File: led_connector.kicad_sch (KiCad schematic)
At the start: 7 parts, among them U3 SM02B-SRSS-TB-LF-SN, U4 SM02B-SRSS-TB-LF-SN

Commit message: Update naming convention
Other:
- title: (none) -> LZ1 OSRAM LuxiGen LED Driver
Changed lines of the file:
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@@
 (kicad_sch (version 20211123) (generator eeschema)
   (paper "A4")
+  (title_block
+    (title "LZ1 OSRAM LuxiGen LED Driver")
+    (date "2023-05-04")
+    (rev "1.0.0")
+    (comment 1 "www.antmicro.com")
+  )
   (junction (at 60.325 114.935) (diameter 0) (color 0 0 0 0)
   )
@@
   (symbol (lib_id "power:GND") (at 60.325 116.205 0) (unit 1)
     (in_bom yes) (on_board yes) (fields_autoplaced)
-    (property "Reference" "#PWR0103" (id 0) (at 60.325 122.555 0)
+    (property "Reference" "#PWR?" (id 0) (at 60.325 122.555 0)
       (effects (font (size 1.27 1.27)) hide)
     )
@@
   (symbol (lib_id "power:GND") (at 219.71 114.935 0) (unit 1)
     (in_bom yes) (on_board yes) (fields_autoplaced)
-    (property "Reference" "#PWR0102" (id 0) (at 219.71 121.285 0)
-      (effects (font (size 1.27 1.27)) hide)
-    )
+    (property "Reference" "#PWR?" (id 0) (at 219.71 121.285 0)
+      (effects (font (size 1.27 1.27)) hide)
+    )

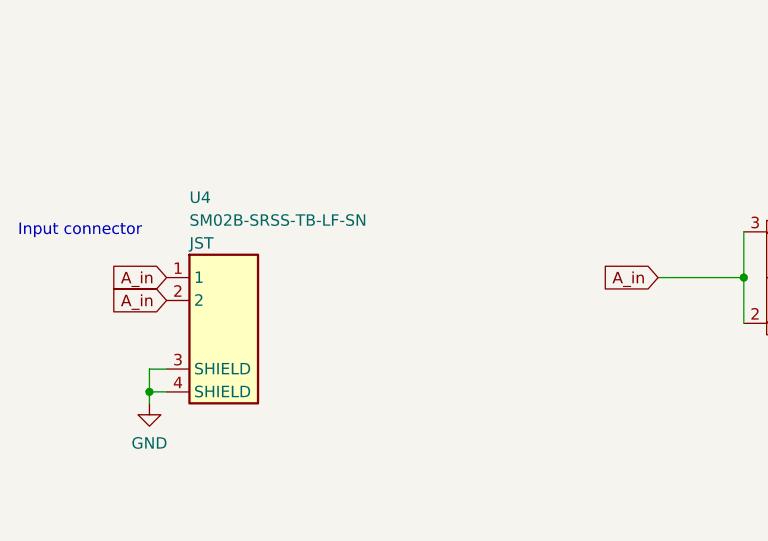
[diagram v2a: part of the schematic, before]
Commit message: Correct sch logos. Update PCB from schematic
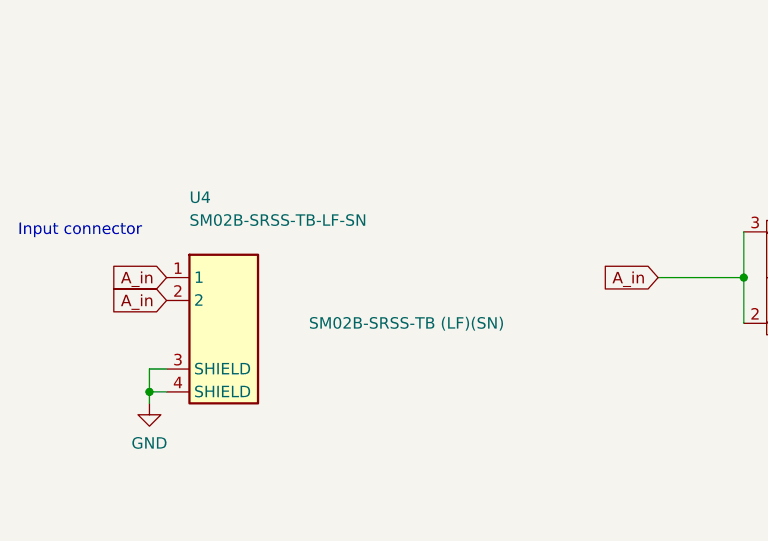
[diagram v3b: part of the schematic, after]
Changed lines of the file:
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@@
   (symbol (lib_id "power:GND") (at 60.325 116.205 0) (unit 1)
     (in_bom yes) (on_board yes) (fields_autoplaced)
-    (property "Reference" "#PWR?" (id 0) (at 60.325 122.555 0)
+    (property "Reference" "#PWR0102" (id 0) (at 60.325 122.555 0)
       (effects (font (size 1.27 1.27)) hide)
     )
@@
   (symbol (lib_id "power:GND") (at 219.71 114.935 0) (unit 1)
     (in_bom yes) (on_board yes) (fields_autoplaced)
-    (property "Reference" "#PWR?" (id 0) (at 219.71 121.285 0)
+    (property "Reference" "#PWR0103" (id 0) (at 219.71 121.285 0)
       (effects (font (size 1.27 1.27)) hide)
     )
@@
       (effects (font (size 1.27 1.27)) hide)
     )
-    (property "MPN" "SM02B-SRSS-TB (LF)(SN)" (id 4) (at 88.9 107.315 0)
-      (effects (font (size 1.27 1.27)) hide)
-    )
+    (property "MPN" "SM02B-SRSS-TB (LF)(SN)" (id 4) (at 88.9 107.315 0))
     (property "Manufacturer" "JST" (id 5) (at 64.77 98.4249 0)
-      (effects (font (size 1.27 1.27)) (justify left))
+      (effects (font (size 1.27 1.27)) (justify left) hide)
     )
     (property "Copyright" "Copyright (c) 2023 Antmicro" (id 6) (at 90.17 109.855 0)

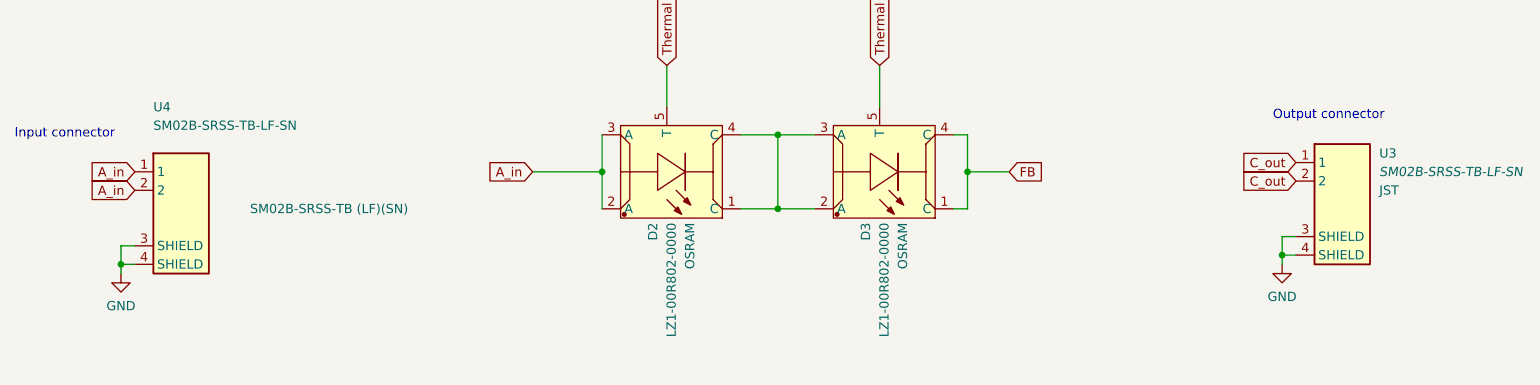
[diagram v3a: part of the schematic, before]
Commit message: Correct symbols and footprints with missing 3D models
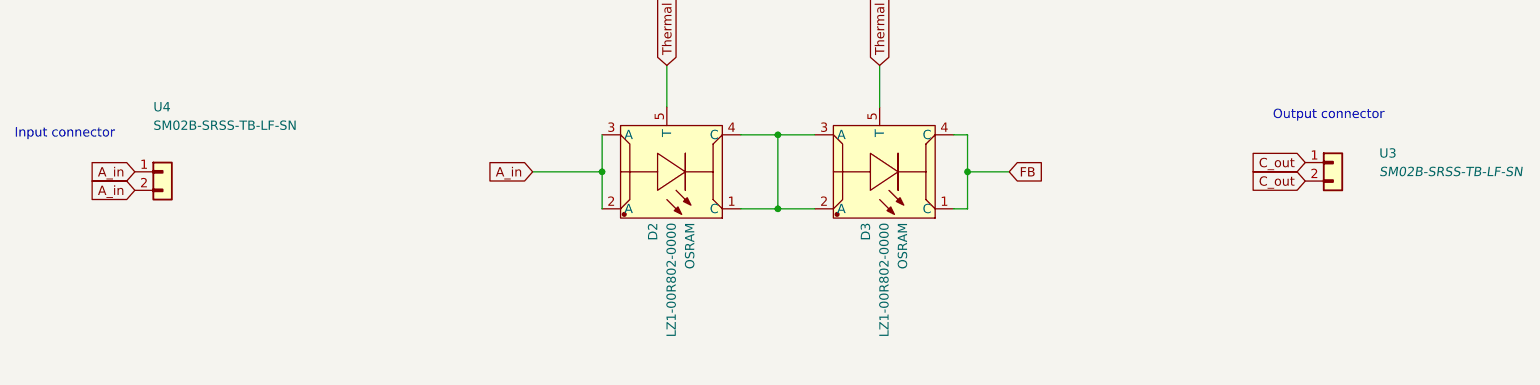
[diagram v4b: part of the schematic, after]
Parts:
- U3, U4: footprint antmicro-footprints:JST_SM02B-SRSS-TB(LF)(SN) -> antmicro-footprints:JST_SM02B-SRSS-TB-LF-SN; Author (none) -> Antmicro; Copyright Copyright (c) 2023 Antmicro -> (none); License Apache-2.0 License -> Apache-2.0; MPN SM02B-SRSS-TB (LF)(SN) -> SM02B-SRSS-TB(LF)(SN)
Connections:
- removed net GND: U3.3 (SHIELD), U3.4 (SHIELD), U4.3 (SHIELD), U4.4 (SHIELD)
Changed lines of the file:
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@@
     (comment 1 "www.antmicro.com")
   )
-  (junction (at 60.325 114.935) (diameter 0) (color 0 0 0 0)
-  )
   (junction (at 144.145 39.37) (diameter 0) (color 0 0 0 0)
   )
   (junction (at 156.21 52.705) (diameter 0) (color 0 0 0 0)
   )
-  (junction (at 219.71 113.665) (diameter 0) (color 0 0 0 0)
-  )
   (junction (at 176.53 102.235) (diameter 0) (color 0 0 0 0)
   )
@@
     (stroke (width 0) (type default) (color 0 0 0 0))
   )
-  (wire (pts (xy 219.71 113.665) (xy 221.615 113.665))
-    (stroke (width 0) (type default) (color 0 0 0 0))
-  )
   (wire (pts (xy 145.415 97.155) (xy 150.495 97.155))
     (stroke (width 0) (type default) (color 0 0 0 0))
@@
     (stroke (width 0) (type default) (color 0 0 0 0))
   )
-  (wire (pts (xy 219.71 113.665) (xy 219.71 114.935))
-    (stroke (width 0) (type default) (color 0 0 0 0))
-  )
   (polyline (pts (xy 163.195 17.78) (xy 163.195 31.115))
     (stroke (width 0) (type default) (color 0 0 0 0))
@@
     (stroke (width 0) (type default) (color 0 0 0 0))
   )
-  (wire (pts (xy 219.71 111.125) (xy 219.71 113.665))
-    (stroke (width 0) (type default) (color 0 0 0 0))
-  )
   (wire (pts (xy 150.495 97.155) (xy 150.495 107.315))
     (stroke (width 0) (type default) (color 0 0 0 0))
@@
     (stroke (width 0) (type default) (color 0 0 0 0))
   )
-  (wire (pts (xy 60.325 114.935) (xy 62.23 114.935))
-    (stroke (width 0) (type default) (color 0 0 0 0))
-  )
   (wire (pts (xy 176.53 107.315) (xy 176.53 102.235))
     (stroke (width 0) (type default) (color 0 0 0 0))
@@
     (stroke (width 0) (type default) (color 0 0 0 0))
   )
-  (wire (pts (xy 60.325 112.395) (xy 60.325 114.935))
-    (stroke (width 0) (type default) (color 0 0 0 0))
-  )
   (wire (pts (xy 144.145 39.37) (xy 144.145 45.085))
     (stroke (width 0) (type default) (color 0 0 0 0))
@@
     (stroke (width 0) (type default) (color 0 0 0 0))
   )
-  (wire (pts (xy 62.23 112.395) (xy 60.325 112.395))
-    (stroke (width 0) (type default) (color 0 0 0 0))
-  )
   (polyline (pts (xy 154.305 17.78) (xy 154.305 31.115))
     (stroke (width 0) (type default) (color 0 0 0 0))
@@
     (stroke (width 0) (type default) (color 0 0 0 0))
   )
-  (wire (pts (xy 221.615 111.125) (xy 219.71 111.125))
-    (stroke (width 0) (type default) (color 0 0 0 0))
-  )
   (wire (pts (xy 156.21 45.085) (xy 156.21 52.705))
     (stroke (width 0) (type default) (color 0 0 0 0))
@@
   )
   (wire (pts (xy 126.365 107.315) (xy 126.365 102.235))
-    (stroke (width 0) (type default) (color 0 0 0 0))
-  )
-  (wire (pts (xy 60.325 114.935) (xy 60.325 116.205))
     (stroke (width 0) (type default) (color 0 0 0 0))
   )
@@
     )
   )
-  (global_label "C_out" (shape input) (at 221.615 100.965 180) (fields_autoplaced)
-    (effects (font (size 1.27 1.27)) (justify right))
-    (property "Intersheet References" "${INTERSHEET_REFS}" (id 0) (at 213.9405 100.8856 0)
+  (global_label "C_out" (shape input) (at 222.885 100.965 180) (fields_autoplaced)
+    (effects (font (size 1.27 1.27)) (justify right))
+    (property "Intersheet References" "${INTERSHEET_REFS}" (id 0) (at 215.2105 100.8856 0)
       (effects (font (size 1.27 1.27)) (justify right) hide)
     )
@@
     )
   )
-  (global_label "C_out" (shape input) (at 221.615 103.505 180) (fields_autoplaced)
-    (effects (font (size 1.27 1.27)) (justify right))
-    (property "Intersheet References" "${INTERSHEET_REFS}" (id 0) (at 213.9405 103.4256 0)
+  (global_label "C_out" (shape input) (at 222.885 103.505 180) (fields_autoplaced)
+    (effects (font (size 1.27 1.27)) (justify right))
+    (property "Intersheet References" "${INTERSHEET_REFS}" (id 0) (at 215.2105 103.4256 0)
       (effects (font (size 1.27 1.27)) (justify right) hide)
     )
@@
     (pin "5")
   )
-  (symbol (lib_id "power:GND") (at 60.325 116.205 0) (unit 1)
-    (in_bom yes) (on_board yes) (fields_autoplaced)
-    (property "Reference" "#PWR0102" (id 0) (at 60.325 122.555 0)
-      (effects (font (size 1.27 1.27)) hide)
-    )
-    (property "Value" "GND" (id 1) (at 60.325 120.65 0))
-    (property "Footprint" "" (id 2) (at 60.325 116.205 0)
-      (effects (font (size 1.27 1.27)) hide)
-    )
-    (property "Datasheet" "" (id 3) (at 60.325 116.205 0)
-      (effects (font (size 1.27 1.27)) hide)
-    )
-    (pin "1")
-  )
   (symbol (lib_id "antmicroRectangularConnectorsHeadersMalePins:SM02B-SRSS-TB-LF-SN") (at 222.885 100.965 0) (unit 1)
     (in_bom yes) (on_board yes) (fields_autoplaced)
@@
       (effects (font (size 1.27 1.27) italic) (justify left))
     )
-    (property "Footprint" "antmicro-footprints:JST_SM02B-SRSS-TB(LF)(SN)" (id 2) (at 260.985 111.125 0)
-      (effects (font (size 1.27 1.27)) hide)
-    )
-    (property "Datasheet" "https://www.farnell.com/datasheets/2082363.pdf" (id 3) (at 260.985 103.505 0)
-      (effects (font (size 1.27 1.27)) hide)
-    )
-    (property "MPN" "SM02B-SRSS-TB (LF)(SN)" (id 4) (at 249.555 106.045 0)
-      (effects (font (size 1.27 1.27)) hide)
-    )
-    (property "Manufacturer" "JST" (id 5) (at 233.045 104.7749 0)
-      (effects (font (size 1.27 1.27)) (justify left))
-    )
-    (property "Copyright" "Copyright (c) 2023 Antmicro" (id 6) (at 250.825 108.585 0)
-      (effects (font (size 1.27 1.27)) hide)
-    )
-    (property "License" "Apache-2.0 License" (id 7) (at 247.015 100.965 0)
-      (effects (font (size 1.27 1.27)) hide)
-    )
-    (pin "1")
-    (pin "2")
-    (pin "3")
-    (pin "4")
-  )
-  (symbol (lib_id "power:GND") (at 219.71 114.935 0) (unit 1)
-    (in_bom yes) (on_board yes) (fields_autoplaced)
-    (property "Reference" "#PWR0103" (id 0) (at 219.71 121.285 0)
-      (effects (font (size 1.27 1.27)) hide)
-    )
-    (property "Value" "GND" (id 1) (at 219.71 119.38 0))
-    (property "Footprint" "" (id 2) (at 219.71 114.935 0)
-      (effects (font (size 1.27 1.27)) hide)
-    )
-    (property "Datasheet" "" (id 3) (at 219.71 114.935 0)
-      (effects (font (size 1.27 1.27)) hide)
-    )
-    (pin "1")
+    (property "Footprint" "antmicro-footprints:JST_SM02B-SRSS-TB-LF-SN" (id 2) (at 249.555 109.855 0)
+      (effects (font (size 1.27 1.27) (thickness 0.15)) (justify left bottom) hide)
+    )
+    (property "Datasheet" "https://www.jst-mfg.com/product/pdf/eng/eSH.pdf" (id 3) (at 249.555 112.395 0)
+      (effects (font (size 1.27 1.27) (thickness 0.15)) (justify left bottom) hide)
+    )
+    (property "MPN" "SM02B-SRSS-TB(LF)(SN)" (id 4) (at 249.555 114.935 0)
+      (effects (font (size 1.27 1.27) (thickness 0.15)) (justify left bottom) hide)
+    )
+    (property "Manufacturer" "JST" (id 5) (at 249.555 117.475 0)
+      (effects (font (size 1.27 1.27) (thickness 0.15)) (justify left bottom) hide)
+    )
+    (property "License" "Apache-2.0" (id 7) (at 249.555 122.555 0)
+      (effects (font (size 1.27 1.27) (thickness 0.15)) (justify left bottom) hide)
+    )
+    (property "Author" "Antmicro" (id 7) (at 249.555 120.015 0)
+      (effects (font (size 1.27 1.27) (thickness 0.15)) (justify left bottom) hide)
+    )
+    (pin "1")
+    (pin "2")
   )
   (symbol (lib_id "antmicroLEDIndicationDiscrete:LZ1-00R802-0000") (at 145.415 107.315 180) (unit 1)
@@
       (effects (font (size 1.27 1.27)) (justify left))
     )
-    (property "Footprint" "antmicro-footprints:JST_SM02B-SRSS-TB(LF)(SN)" (id 2) (at 100.33 112.395 0)
-      (effects (font (size 1.27 1.27)) hide)
-    )
-    (property "Datasheet" "https://www.farnell.com/datasheets/2082363.pdf" (id 3) (at 100.33 104.775 0)
-      (effects (font (size 1.27 1.27)) hide)
-    )
-    (property "MPN" "SM02B-SRSS-TB (LF)(SN)" (id 4) (at 88.9 107.315 0))
-    (property "Manufacturer" "JST" (id 5) (at 64.77 98.4249 0)
-      (effects (font (size 1.27 1.27)) (justify left) hide)
-    )
-    (property "Copyright" "Copyright (c) 2023 Antmicro" (id 6) (at 90.17 109.855 0)
-      (effects (font (size 1.27 1.27)) hide)
-    )
-    (property "License" "Apache-2.0 License" (id 7) (at 86.36 102.235 0)
-      (effects (font (size 1.27 1.27)) hide)
-    )
-    (pin "1")
-    (pin "2")
-    (pin "3")
-    (pin "4")
+    (property "Footprint" "antmicro-footprints:JST_SM02B-SRSS-TB-LF-SN" (id 2) (at 88.9 111.125 0)
+      (effects (font (size 1.27 1.27) (thickness 0.15)) (justify left bottom) hide)
+    )
+    (property "Datasheet" "https://www.jst-mfg.com/product/pdf/eng/eSH.pdf" (id 3) (at 88.9 113.665 0)
+      (effects (font (size 1.27 1.27) (thickness 0.15)) (justify left bottom) hide)
+    )
+    (property "MPN" "SM02B-SRSS-TB(LF)(SN)" (id 4) (at 88.9 116.205 0)
+      (effects (font (size 1.27 1.27) (thickness 0.15)) (justify left bottom) hide)
+    )
+    (property "Manufacturer" "JST" (id 5) (at 88.9 118.745 0)
+      (effects (font (size 1.27 1.27) (thickness 0.15)) (justify left bottom) hide)
+    )
+    (property "License" "Apache-2.0" (id 7) (at 88.9 123.825 0)
+      (effects (font (size 1.27 1.27) (thickness 0.15)) (justify left bottom) hide)
+    )
+    (property "Author" "Antmicro" (id 7) (at 88.9 121.285 0)
+      (effects (font (size 1.27 1.27) (thickness 0.15)) (justify left bottom) hide)
+    )
+    (pin "1")
+    (pin "2")
   )
 )

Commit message: Refresh standardization on schematic and PCB
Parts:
- D2, D3: footprint antmicro-footprints:LZ1-00R802_4EP_4.4x4.4 -> antmicro-footprints:LED_IR_LZ1-00R802; symbol antmicroLEDIndicationDiscrete:LZ1-00R802-0000 -> antmicroLEDIndicationDiscrete:LED_IR_LZ1-00R802; Author (none) -> Antmicro; License Apache-2.0 License -> Apache-2.0; Manufacturer OSRAM -> Osram
- R10, R11, R7: Author (none) -> Antmicro; Copyright Copyright (c) 2023 Antmicro -> (none); License Apache-2.0 License -> Apache-2.0; Manufacturer Multicomp PRO -> Multicomp
- renumbered U3 to J3, U4 to J4

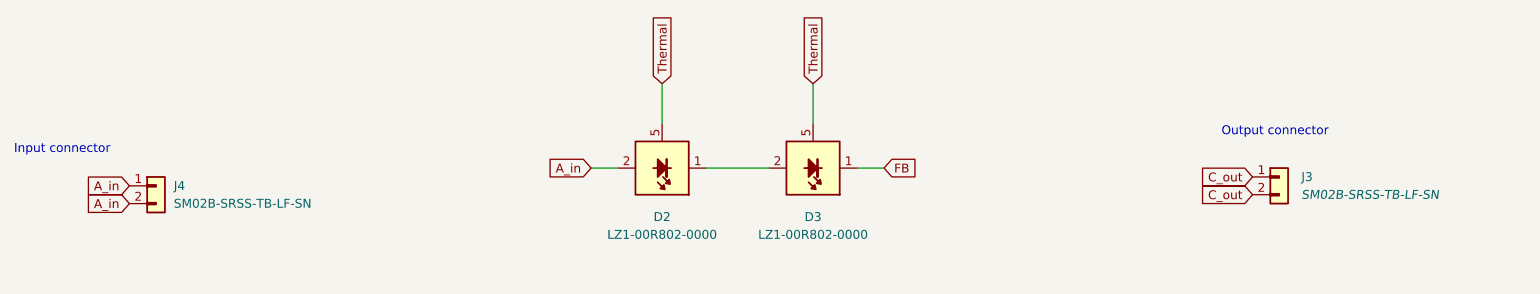
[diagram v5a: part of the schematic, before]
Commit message: Introduced schematic standardization
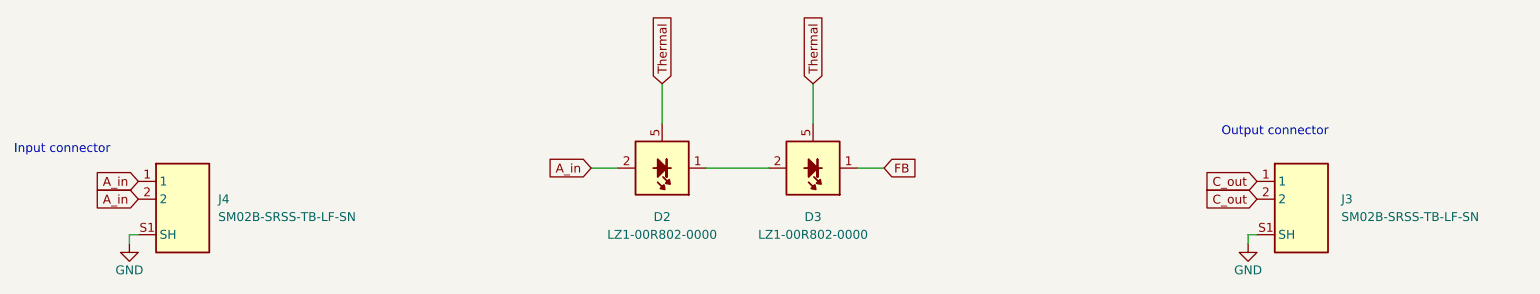
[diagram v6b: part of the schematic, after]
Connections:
- new net GND: J3.S1 (SH), J3.S2 (SH), J4.S1 (SH), J4.S2 (SH)
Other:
- company: (none) -> Antmicro Ltd.
